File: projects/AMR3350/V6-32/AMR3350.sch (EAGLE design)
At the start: 241 parts, among them IC1 LDO-TS1117CW-3V3, IC10 TMC21X0-LA, IC11 74LS32D, IC2 ATSAM4S8C, IC3 SI87XXIS, IC4 74HC125, IC5 74S08D, IC6 TMC21X0-LA, IC7 TMC21X0-LA, IC8 TMC21X0-LA, IC9 TMC21X0-LA, J1 MOLEX-105162-001, J2 MSTBV4, Q1 NX138BKS, Q2 NX138BKS, Q3 BUK9Y53-100B, Q4 BUK9Y53-100B, U1 A4403, X1 USB-B_TH, X2 12MHz, X3 KK-254-2, X4 KK-254-4, X5 KK-254-4, X6 KK-254-4, X7 KK-254-4, X8 KK-254-4, X9 KK-254-4

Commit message: More progress
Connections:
- net FAN1_D1 renamed FAN3_D
- net FAN1_G1 renamed FAN3_G
- net FAN2_D1 renamed FAN4_D
- net FAN2_G1 renamed FAN4_G
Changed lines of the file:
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@@
 <grid distance="0.1" unitdist="inch" unit="inch" style="lines" multiple="1" display="no" altdistance="0.01" altunitdist="inch" altunit="inch"/>
 <layers>
-<layer number="1" name="Top" color="4" fill="1" visible="yes" active="no"/>
-<layer number="2" name="Route2" color="16" fill="1" visible="yes" active="no"/>
-<layer number="3" name="Route3" color="17" fill="1" visible="yes" active="no"/>
-<layer number="4" name="Route4" color="18" fill="1" visible="yes" active="no"/>
-<layer number="5" name="Route5" color="19" fill="1" visible="yes" active="no"/>
-<layer number="6" name="Route6" color="25" fill="1" visible="yes" active="no"/>
-<layer number="7" name="Route7" color="26" fill="1" visible="yes" active="no"/>
-<layer number="8" name="Route8" color="27" fill="1" visible="yes" active="no"/>
-<layer number="9" name="Route9" color="28" fill="1" visible="yes" active="no"/>
-<layer number="10" name="Route10" color="29" fill="1" visible="yes" active="no"/>
-<layer number="11" name="Route11" color="30" fill="1" visible="yes" active="no"/>
-<layer number="12" name="Route12" color="20" fill="1" visible="yes" active="no"/>
-<layer number="13" name="Route13" color="21" fill="1" visible="yes" active="no"/>
-<layer number="14" name="Route14" color="22" fill="1" visible="yes" active="no"/>
-<layer number="15" name="Route15" color="23" fill="1" visible="yes" active="no"/>
-<layer number="16" name="Bottom" color="1" fill="1" visible="yes" active="no"/>
-<layer number="17" name="Pads" color="2" fill="1" visible="yes" active="no"/>
-<layer number="18" name="Vias" color="2" fill="1" visible="yes" active="no"/>
-<layer number="19" name="Unrouted" color="6" fill="1" visible="yes" active="no"/>
-<layer number="20" name="Dimension" color="24" fill="1" visible="yes" active="no"/>
-<layer number="21" name="tPlace" color="7" fill="1" visible="yes" active="no"/>
-<layer number="22" name="bPlace" color="7" fill="1" visible="yes" active="no"/>
-<layer number="23" name="tOrigins" color="15" fill="1" visible="yes" active="no"/>
-<layer number="24" name="bOrigins" color="15" fill="1" visible="yes" active="no"/>
-<layer number="25" name="tNames" color="7" fill="1" visible="yes" active="no"/>
-<layer number="26" name="bNames" color="7" fill="1" visible="yes" active="no"/>
-<layer number="27" name="tValues" color="7" fill="1" visible="yes" active="no"/>
-<layer number="28" name="bValues" color="7" fill="1" visible="yes" active="no"/>
+<layer number="1" name="Top" color="4" fill="1" visible="no" active="no"/>
+<layer number="2" name="Route2" color="16" fill="1" visible="no" active="no"/>
+<layer number="3" name="Route3" color="17" fill="1" visible="no" active="no"/>
+<layer number="4" name="Route4" color="18" fill="1" visible="no" active="no"/>
+<layer number="5" name="Route5" color="19" fill="1" visible="no" active="no"/>
+<layer number="6" name="Route6" color="25" fill="1" visible="no" active="no"/>
+<layer number="7" name="Route7" color="26" fill="1" visible="no" active="no"/>
+<layer number="8" name="Route8" color="27" fill="1" visible="no" active="no"/>
+<layer number="9" name="Route9" color="28" fill="1" visible="no" active="no"/>
+<layer number="10" name="Route10" color="29" fill="1" visible="no" active="no"/>
+<layer number="11" name="Route11" color="30" fill="1" visible="no" active="no"/>
+<layer number="12" name="Route12" color="20" fill="1" visible="no" active="no"/>
+<layer number="13" name="Route13" color="21" fill="1" visible="no" active="no"/>
+<layer number="14" name="Route14" color="22" fill="1" visible="no" active="no"/>
+<layer number="15" name="Route15" color="23" fill="1" visible="no" active="no"/>
+<layer number="16" name="Bottom" color="1" fill="1" visible="no" active="no"/>
+<layer number="17" name="Pads" color="2" fill="1" visible="no" active="no"/>
+<layer number="18" name="Vias" color="2" fill="1" visible="no" active="no"/>
+<layer number="19" name="Unrouted" color="6" fill="1" visible="no" active="no"/>
+<layer number="20" name="Dimension" color="24" fill="1" visible="no" active="no"/>
+<layer number="21" name="tPlace" color="7" fill="1" visible="no" active="no"/>
+<layer number="22" name="bPlace" color="7" fill="1" visible="no" active="no"/>
+<layer number="23" name="tOrigins" color="15" fill="1" visible="no" active="no"/>
+<layer number="24" name="bOrigins" color="15" fill="1" visible="no" active="no"/>
+<layer number="25" name="tNames" color="7" fill="1" visible="no" active="no"/>
+<layer number="26" name="bNames" color="7" fill="1" visible="no" active="no"/>
+<layer number="27" name="tValues" color="7" fill="1" visible="no" active="no"/>
+<layer number="28" name="bValues" color="7" fill="1" visible="no" active="no"/>
 <layer number="29" name="tStop" color="7" fill="3" visible="no" active="no"/>
 <layer number="30" name="bStop" color="7" fill="6" visible="no" active="no"/>
@@
 <layer number="35" name="tGlue" color="7" fill="4" visible="no" active="no"/>
 <layer number="36" name="bGlue" color="7" fill="5" visible="no" active="no"/>
-<layer number="37" name="tTest" color="7" fill="1" visible="yes" active="no"/>
-<layer number="38" name="bTest" color="7" fill="1" visible="yes" active="no"/>
+<layer number="37" name="tTest" color="7" fill="1" visible="no" active="no"/>
+<layer number="38" name="bTest" color="7" fill="1" visible="no" active="no"/>
 <layer number="39" name="tKeepout" color="4" fill="11" visible="no" active="no"/>
 <layer number="40" name="bKeepout" color="1" fill="11" visible="no" active="no"/>
@@
 <layer number="44" name="Drills" color="7" fill="1" visible="no" active="no"/>
 <layer number="45" name="Holes" color="7" fill="1" visible="no" active="no"/>
-<layer number="46" name="Milling" color="3" fill="1" visible="yes" active="no"/>
-<layer number="47" name="Measures" color="7" fill="1" visible="yes" active="no"/>
-<layer number="48" name="Document" color="7" fill="1" visible="yes" active="no"/>
-<layer number="49" name="Reference" color="7" fill="1" visible="yes" active="no"/>
-<layer number="50" name="dxf" color="7" fill="1" visible="yes" active="no"/>
-<layer number="51" name="tDocu" color="7" fill="1" visible="yes" active="no"/>
-<layer number="52" name="bDocu" color="7" fill="1" visible="yes" active="no"/>
-<layer number="53" name="tGND_GNDA" color="7" fill="9" visible="yes" active="no"/>
-<layer number="54" name="bGND_GNDA" color="1" fill="9" visible="yes" active="no"/>
-<layer number="56" name="wert" color="7" fill="1" visible="yes" active="no"/>
-<layer number="57" name="tCAD" color="7" fill="1" visible="yes" active="no"/>
-<layer number="59" name="tCarbon" color="7" fill="1" visible="yes" active="no"/>
-<layer number="60" name="bCarbon" color="7" fill="1" visible="yes" active="no"/>
+<layer number="46" name="Milling" color="3" fill="1" visible="no" active="no"/>
+<layer number="47" name="Measures" color="7" fill="1" visible="no" active="no"/>
+<layer number="48" name="Document" color="7" fill="1" visible="no" active="no"/>
+<layer number="49" name="Reference" color="7" fill="1" visible="no" active="no"/>
+<layer number="50" name="dxf" color="7" fill="1" visible="no" active="no"/>
+<layer number="51" name="tDocu" color="7" fill="1" visible="no" active="no"/>
+<layer number="52" name="bDocu" color="7" fill="1" visible="no" active="no"/>
+<layer number="53" name="tGND_GNDA" color="7" fill="9" visible="no" active="no"/>
+<layer number="54" name="bGND_GNDA" color="1" fill="9" visible="no" active="no"/>
+<layer number="56" name="wert" color="7" fill="1" visible="no" active="no"/>
+<layer number="57" name="tCAD" color="7" fill="1" visible="no" active="no"/>
+<layer number="59" name="tCarbon" color="7" fill="1" visible="no" active="no"/>
+<layer number="60" name="bCarbon" color="7" fill="1" visible="no" active="no"/>
 <layer number="88" name="SimResults" color="9" fill="1" visible="yes" active="yes"/>
 <layer number="89" name="SimProbes" color="9" fill="1" visible="yes" active="yes"/>
@@
 </segment>
 </net>
-<net name="FAN2_D1" class="0">
+<net name="FAN4_D" class="0">
 <segment>
 <wire x1="868.68" y1="33.02" x2="901.7" y2="33.02" width="0.1524" layer="91"/>
@@
 </segment>
 </net>
-<net name="FAN1_D1" class="0">
+<net name="FAN3_D" class="0">
 <segment>
 <wire x1="868.68" y1="48.26" x2="901.7" y2="48.26" width="0.1524" layer="91"/>
@@
 </segment>
 </net>
-<net name="FAN1_G1" class="0">
+<net name="FAN3_G" class="0">
 <segment>
 <wire x1="863.6" y1="40.64" x2="861.06" y2="40.64" width="0.1524" layer="91"/>
@@
 </segment>
 </net>
-<net name="FAN2_G1" class="0">
+<net name="FAN4_G" class="0">
 <segment>
 <wire x1="863.6" y1="25.4" x2="861.06" y2="25.4" width="0.1524" layer="91"/>

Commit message: Some traces
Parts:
- added F2, F3: (no value), fuse:19560
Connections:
- net EXT_D renamed EXT1_D
- net EXT_G renamed EXT1_G
- removed net ADVREF1: C24.1, IC2.ADVREF, L4.1
- new net N$1: F2.2, J2-2.1
- new net N$2: F3.2, J2-4.1
- new net N$3: X6-1.S, X9-2.S
- new net N$4: X6-4.S, X9-3.S
- net +12V: now also F2.1, F3.1; no longer J2-2.1, J2-4.1
- net A1_Z: no longer X6-1.S
- net A2_Z: no longer X9-2.S
- net ADVREF: now also C24.1, IC2.ADVREF, L4.1
- net B1_Z: no longer X9-3.S
- net B2_Z: no longer X6-4.S
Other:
- moved on the sheet: J2-1, J2-2, J2-3, J2-4, X6-1, X6-2, X6-3, X6-4

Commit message: Almost done*
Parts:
- D1: device diode:SCHOTTKY-DIODESMC -> diode:SCHOTTKY-DIODESMD
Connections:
- removed net N$6: IC11A.O, IC11C.I1
- new net ESP_RST: ESP1.RESET, R18.2, R22.2
- new net N$5: IC11B.O, IC11C.I1
- net ESP_RESET: no longer ESP1.RESET, R18.2, R22.2
- net GND: now also IC5C.I0, IC5C.I1; no longer IC5A.I0, IC5A.I1
- net LCD_CS: now also IC5A.I1; no longer IC5C.I1
- net LCD_ENC_A: now also IC2.TCK/SWCLK/PB7; no longer IC2.PC20
- net LCD_ENC_B: now also IC2.PC20; no longer IC2.TCK/SWCLK/PB7
- net LCD_MOSI: now also IC5A.I0; no longer IC5C.I0
- net LCD_MOSI_BUF: now also IC5A.O; no longer IC5C.O
- net N$7: now also IC11A.O; no longer IC11B.O
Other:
- moved on the sheet: IC5A, IC5C

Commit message: Almost** done*
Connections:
- net BED: now also IC2.PC22; no longer IC2.PC0
- net ESP_DATA_RDY: now also IC2.PC26; no longer IC2.PC3
- net FAN_E1: now also IC2.PC3; no longer IC2.PB13/DAC0
- net FAN_E2: now also IC2.PC0; no longer IC2.PC22
- net PWR_FAIL_DET2: now also IC2.PC30/AD14; no longer IC2.PC12/AD12
- net X_STOP: now also IC2.PC16
- net Y_STOP: now also IC2.PA0/PGMEN0
- net Z_STOP: now also IC2.PC17

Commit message: Done***
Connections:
- net RESET: now also RESET.P1; no longer RESET.P
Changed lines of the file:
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@@
 <wire x1="332.74" y1="-33.02" x2="332.74" y2="-30.48" width="0.1524" layer="91"/>
 <junction x="332.74" y="-30.48"/>
-<pinref part="RESET" gate="G$1" pin="P"/>
-<wire x1="332.74" y1="-30.48" x2="332.74" y2="-27.94" width="0.1524" layer="91"/>
-<wire x1="332.74" y1="-27.94" x2="335.28" y2="-27.94" width="0.1524" layer="91"/>
 <label x="297.18" y="-30.48" size="1.778" layer="95"/>
+<pinref part="RESET" gate="G$1" pin="P1"/>
+<wire x1="332.74" y1="-30.48" x2="335.28" y2="-30.48" width="0.1524" layer="91"/>
 </segment>
 </net>

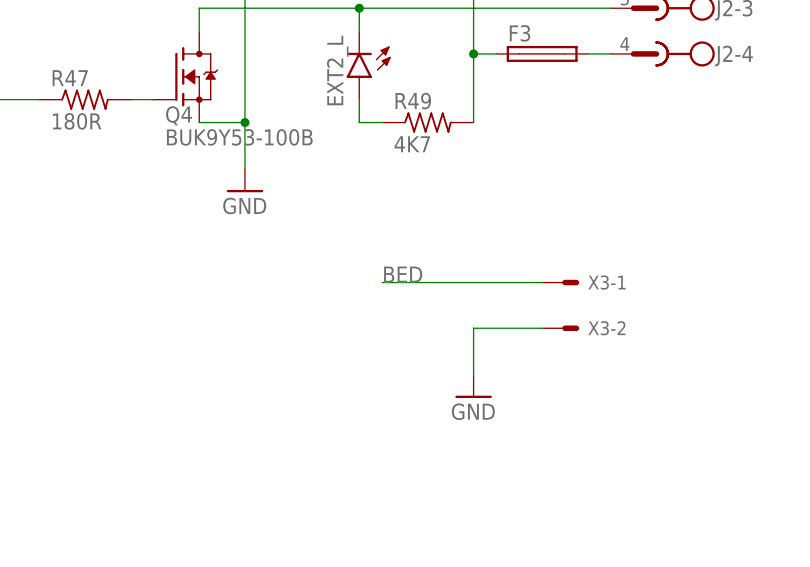
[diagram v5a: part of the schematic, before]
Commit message: Added a resistor
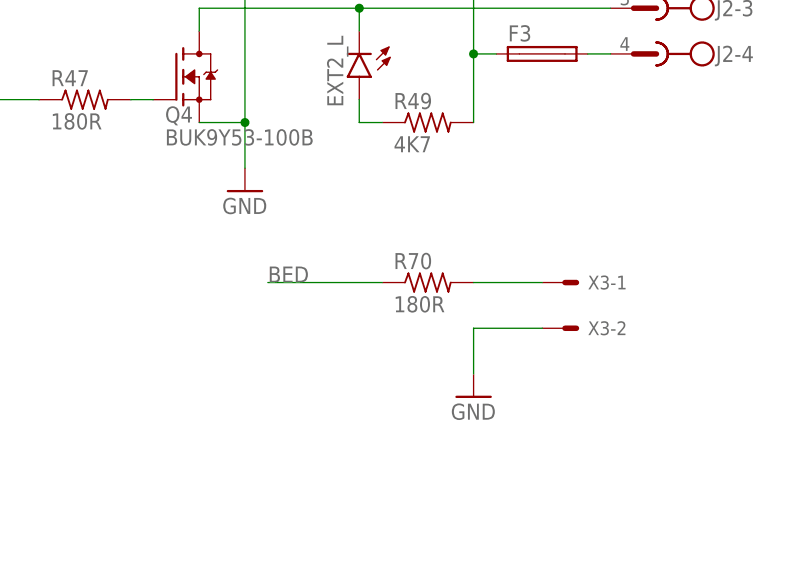
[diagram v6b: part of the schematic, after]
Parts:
- added R70: 180R, resistor:R-US_R0603
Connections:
- new net BED_OUT: R70.2, X3-1.S
- net BED: now also R70.1; no longer X3-1.S

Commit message: Properly positioned names/labels (silkscreen)
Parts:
- removed U1: A4403, misc:A4403
- removed X1: USB-B_TH, SmartPrj:PN61729
- added IC12: 74LS32D, 74xx-us:74LS32D
- added USB_L: (no value), led:LEDCHIPLED_0805
- IC1: value LDO-TS1117CW-3V3 -> A4403; device we-power:LDO-TS1117CW-3V3 -> misc:A4403
- IC11: value 74LS32D -> TMC21X0-LA; device 74xx-us:74LS32D -> SilentStepStick-TMC2130_v11:TMC21X0-LA
- IC2: value ATSAM4S8C -> LDO-TS1117CW-3V3; device misc:ATSAM4S8C -> we-power:LDO-TS1117CW-3V3
- IC3: value SI87XXIS -> ATSAM4S8C; device misc:SI87XXIS -> misc:ATSAM4S8C
- IC4: value 74HC125 -> SI87XXIS; device misc:74HC125 -> misc:SI87XXIS
- IC5: value 74S08D -> 74HC125; device 74xx-us:74S08D -> misc:74HC125
- IC6: value TMC21X0-LA -> 74S08D; device SilentStepStick-TMC2130_v11:TMC21X0-LA -> 74xx-us:74S08D
- R50: value 0R11 -> 180R; device resistor:R-US_R1206 -> resistor:R-US_R0603
- R52, R56, R60, R64, R68: value 20K -> 0R11; device resistor:R-TRIMM3103 -> resistor:R-US_R1206
- R53, R57, R61, R65, R69: device resistor:R-US_R0603 -> resistor:R-TRIMM3103
- R54, R58, R62, R66: value 0R11 -> 20K; device resistor:R-US_R1206 -> resistor:R-US_R0603
- R70: value 180R -> 20K
- USB: value (none) -> USB-B_TH; device led:LEDCHIPLED_0805 -> SmartPrj:PN61729
- renumbered 3V1 to 3V3, ESP1 to ESP8266
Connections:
- net ESP_URDX renamed ESP_RXD
- net ESP_UTDX renamed ESP_TXD
- net N$1 renamed E1_FUSED
- net N$2 renamed E2_FUSED
- net N$55 renamed IDEK
- removed net N$3: X6-1.S, X9-2.S
- removed net N$4: X6-4.S, X9-3.S
- removed net N$5: IC11B.O, IC11C.I1
- removed net N$7: IC11A.O, IC11D.I0
- removed net N$8: IC11C.O, IC11D.I1
- new net AMID_Z: X6-1.S, X7-2.S
- new net BMID_Z: X6-4.S, X7-3.S
- new net SG_TST_E1Z: IC12B.O, IC12C.I1
- new net SG_TST_XY: IC12A.O, IC12D.I0
- new net SG_TST_ZE: IC12C.O, IC12D.I1
- net +12V: now also IC11.VS, IC11.VSA; no longer IC6.VS, IC6.VSA
- net +3V3: now also IC11.VCC_IO, IC12P.VCC, IC2.VO, IC3.VDDIN, IC3.VDDIO-27, IC3.VDDIO-50, IC3.VDDIO-69, IC3.VDDIO-91, IC3.VDDIO-98, IC4.VDD, IC5P.VCC; no longer IC1.VO, IC11P.VCC, IC2.VDDIN, IC2.VDDIO-27, IC2.VDDIO-50, IC2.VDDIO-69, IC2.VDDIO-91, IC2.VDDIO-98, IC3.VDD, IC4P.VCC, IC6.VCC_IO
- net +5V: now also IC11.VCC, IC2.VI, IC6P.VCC, R54.2, R58.2, R62.2, R66.2, R70.2; no longer IC1.VI, IC5P.VCC, IC6.VCC, R53.2, R57.2, R61.2, R65.2, R69.2
- net 5V_E1: now also IC10.5VOUT; no longer IC9.5VOUT
- net 5V_E2: now also IC11.5VOUT; no longer IC10.5VOUT
- net 5V_X: now also IC7.5VOUT; no longer IC6.5VOUT
- net 5V_Y: now also IC8.5VOUT; no longer IC7.5VOUT
- net 5V_Z: now also IC9.5VOUT; no longer IC8.5VOUT
- net A1_E1: now also IC10.OA1, X8-1.S; no longer IC9.OA1, X7-1.S
- net A1_E2: now also IC11.OA1, X9-1.S; no longer IC10.OA1, X8-1.S
- net A1_X: now also IC7.OA1; no longer IC6.OA1
- net A1_Y: now also IC8.OA1; no longer IC7.OA1
- net A1_Z: now also IC9.OA1, X7-1.S; no longer IC8.OA1, X9-1.S
- net A2_E1: now also IC10.OA2, X8-2.S; no longer IC9.OA2, X7-2.S
- net A2_E2: now also IC11.OA2, X9-2.S; no longer IC10.OA2, X8-2.S
- net A2_X: now also IC7.OA2; no longer IC6.OA2
- net A2_Y: now also IC8.OA2; no longer IC7.OA2
- net A2_Z: now also IC9.OA2; no longer IC8.OA2
- net ADVREF: now also IC3.ADVREF; no longer IC2.ADVREF
- net B1_E1: now also IC10.OB1, X8-3.S; no longer IC9.OB1, X7-3.S
- net B1_E2: now also IC11.OB1, X9-3.S; no longer IC10.OB1, X8-3.S
- net B1_X: now also IC7.OB1; no longer IC6.OB1
- net B1_Y: now also IC8.OB1; no longer IC7.OB1
- net B1_Z: now also IC9.OB1; no longer IC8.OB1
- net B2_E1: now also IC10.OB2, X8-4.S; no longer IC9.OB2, X7-4.S
- net B2_E2: now also IC11.OB2, X9-4.S; no longer IC10.OB2, X8-4.S
- net B2_X: now also IC7.OB2; no longer IC6.OB2
- net B2_Y: now also IC8.OB2; no longer IC7.OB2
- net B2_Z: now also IC9.OB2, X7-4.S; no longer IC8.OB2, X9-4.S
- net BED: now also IC3.PC22, R50.1; no longer IC2.PC22, R70.1
- net BED_OUT: now also R50.2; no longer R70.2
- net BOOT: now also IC1.BOOT; no longer U1.BOOT
- net BRA_E1: now also IC10.BRA, R63.1; no longer IC9.BRA, R62.1
- net BRA_E2: now also IC11.BRA, R67.1; no longer IC10.BRA, R66.1
- net BRA_X: now also IC7.BRA, R51.1; no longer IC6.BRA, R50.1
- net BRA_Y: now also IC8.BRA, R55.1; no longer IC7.BRA, R54.1
- net BRA_Z: now also IC9.BRA, R59.1; no longer IC8.BRA, R58.1
- net BRB_E1: now also IC10.BRB, R64.1; no longer IC9.BRB, R63.1
- net BRB_E2: now also IC11.BRB, R68.1; no longer IC10.BRB, R67.1
- net BRB_X: now also IC7.BRB, R52.1; no longer IC6.BRB, R51.1
- net BRB_Y: now also IC8.BRB, R56.1; no longer IC7.BRB, R55.1
- net BRB_Z: now also IC9.BRB, R60.1; no longer IC8.BRB, R59.1
- net CPI_E1: now also IC10.CPI; no longer IC9.CPI
- net CPI_E2: now also IC11.CPI; no longer IC10.CPI
- net CPI_X: now also IC7.CPI; no longer IC6.CPI
- net CPI_Y: now also IC8.CPI; no longer IC7.CPI
- net CPI_Z: now also IC9.CPI; no longer IC8.CPI
- net CPO_E1: now also IC10.CPO; no longer IC9.CPO
- net CPO_E2: now also IC11.CPO; no longer IC10.CPO
- net CPO_X: now also IC7.CPO; no longer IC6.CPO
- net CPO_Y: now also IC8.CPO; no longer IC7.CPO
- net CPO_Z: now also IC9.CPO; no longer IC8.CPO
- net E1_DIR: now also IC10.REFR_DIR, IC3.TDI/PB4; no longer IC2.TDI/PB4, IC9.REFR_DIR
- net E1_EN: now also IC10.CSN_CFG3, IC3.PA4/PGMNCMD; no longer IC2.PA4/PGMNCMD, IC9.CSN_CFG3
- net E1_STEP: now also IC10.REFL_STEP, IC3.PC28; no longer IC2.PC28, IC9.REFL_STEP
- net E2_DIR: now also IC11.REFR_DIR, IC3.PC9; no longer IC10.REFR_DIR, IC2.PC9
- net E2_EN: now also IC11.CSN_CFG3, IC3.PA3; no longer IC10.CSN_CFG3, IC2.PA3
- net E2_STEP: now also IC11.REFL_STEP, IC3.PC10; no longer IC10.REFL_STEP, IC2.PC10
- net ENN: now also IC11.DRV_ENN_CFG6, IC3.PC14; no longer IC2.PC14, IC6.DRV_ENN_CFG6
- net ERASE: now also IC3.ERASE/PB12; no longer IC2.ERASE/PB12
- net ESP_DATA_RDY: now also IC3.PC26; no longer IC2.PC26
- net ESP_EN: now also IC3.PC6; no longer IC2.PC6
- net ESP_MISO: now also IC3.PA12/PGMD0; no longer IC2.PA12/PGMD0
- net ESP_MOSI: now also IC3.PA13/PGMD1; no longer IC2.PA13/PGMD1
- net ESP_NPCS0: now also IC3.PA11/PGMM3; no longer IC2.PA11/PGMM3
- net ESP_RESET: now also IC3.PC2; no longer IC2.PC2
- net ESP_SCK: now also IC3.PA14/PGMD2; no longer IC2.PA14/PGMD2
- net ESP_URXD: now also IC3.PA9/PGMM1; no longer IC2.PA9/PGMM1
- net ESP_UTXD: now also IC3.PA10/PGMM2; no longer IC2.PA10/PGMM2
- net EXT1: now also IC3.PA20/PGMD8/AD3; no longer IC2.PA20/PGMD8/AD3
- net EXT2: now also IC3.PC15/AD11; no longer IC2.PC15/AD11
- net FAN_E1: now also IC3.PC3; no longer IC2.PC3
- net FAN_E2: now also IC3.PC0; no longer IC2.PC0
- net FAN_MOBO: now also IC3.PA18/PGMD6/AD1; no longer IC2.PA18/PGMD6/AD1
- net FAN_PART: now also IC3.PC13/AD10; no longer IC2.PC13/AD10
- net FB: now also IC1.FB; no longer U1.FB
- net GND: now also IC1.DIS, IC1.NC13, IC1.NC14, IC1.NC15, IC1.NC16, IC1.NC2, IC1.NC7, IC1.PAD, IC11.CLK, IC11.ENCB_DCEN_CFG4, IC11.GND, IC11.GNDA, IC11.TST_MODE, IC12P.GND, IC2.GND, IC3.GND-2, IC3.GND-26, IC3.GND-45, IC3.GND-70, IC3.GND-95, IC3.JTAGSEL, IC3.TST, IC4.C1, IC4.GND, IC5A.OE, IC5B.OE, IC5D.I, IC5D.OE, IC6C.I0, IC6C.I1, IC6P.GND, R52.2, R53.E, R56.2, R57.E, R60.2, R61.E, R64.2, R65.E, R68.2, R69.E, USB.4, USB.P$1, USB.P$2; no longer IC11P.GND, IC2.GND-2, IC2.GND-26, IC2.GND-45, IC2.GND-70, IC2.GND-95, IC2.JTAGSEL, IC2.TST, IC3.C1, IC3.GND, IC4A.OE, IC4B.OE, IC4D.I, IC4D.OE, IC4P.GND, IC5C.I0, IC5C.I1, IC6.CLK, IC6.ENCB_DCEN_CFG4, IC6.GND, IC6.GNDA, IC6.TST_MODE, R50.2, R52.E, R54.2, R56.E, R58.2, R60.E, R62.2, R64.E, R66.2, R68.E, U1.DIS, U1.GND, U1.NC13, U1.NC14, U1.NC15, U1.NC16, U1.NC2, U1.NC7, U1.PAD, X1.4, X1.P$1, X1.P$2
- net IREF_E1: now also IC10.AIN_IREF, R65.S; no longer IC9.AIN_IREF, R64.S
- net IREF_E2: now also IC11.AIN_IREF, R69.S; no longer IC10.AIN_IREF, R68.S
- net IREF_X: now also IC7.AIN_IREF, R53.S; no longer IC6.AIN_IREF, R52.S
- net IREF_Y: now also IC8.AIN_IREF, R57.S; no longer IC7.AIN_IREF, R56.S
- net IREF_Z: now also IC9.AIN_IREF, R61.S; no longer IC8.AIN_IREF, R60.S
- net ISEN: now also IC1.ISEN; no longer U1.ISEN
- net LCD_BEEP: now also IC3.PC23; no longer IC2.PC23
- net LCD_CS: now also IC3.PC19, IC6A.I1, IC6B.I0, IC6B.I1, IC6D.I1; no longer IC2.PC19, IC5A.I1, IC5B.I0, IC5B.I1, IC5D.I1
- net LCD_CS_BUF: now also IC6B.O; no longer IC5B.O
- net LCD_ENC_A: now also IC3.TCK/SWCLK/PB7; no longer IC2.TCK/SWCLK/PB7
- net LCD_ENC_B: now also IC3.PC20; no longer IC2.PC20
- net LCD_ENC_SW: now also IC3.PC21; no longer IC2.PC21
- net LCD_MISO: now also IC3.PA5/PGMRDY, IC5C.O; no longer IC2.PA5/PGMRDY, IC4C.O
- net LCD_MISO_BUF: now also IC5C.I; no longer IC4C.I
- net LCD_MOSI: now also IC3.PB6/PGMNOE, IC5A.I, IC6A.I0; no longer IC2.PB6/PGMNOE, IC4A.I, IC5A.I0
- net LCD_MOSI_BUF: now also IC6A.O; no longer IC5A.O
- net LCD_SCK: now also IC3.PA2/PGMEN2, IC5B.I, IC6D.I0; no longer IC2.PA2/PGMEN2, IC4B.I, IC5D.I0
- net LCD_SCK_BUF: now also IC6D.O; no longer IC5D.O
- net LCD_SD_CS: now also IC3.PB14/DAC1, IC5C.OE; no longer IC2.PB14/DAC1, IC4C.OE
- net LX: now also IC1.LX; no longer U1.LX
- net MCCDA: now also IC3.PA28; no longer IC2.PA28
- net MCCK: now also IC3.PA29; no longer IC2.PA29
- net MCDA0: now also IC3.PA30; no longer IC2.PA30
- net MCDA1: now also IC3.PA31; no longer IC2.PA31
- net MCDA2: now also IC3.PA26/PGMD14; no longer IC2.PA26/PGMD14
- net MCDA3: now also IC3.PA27/PGMD15; no longer IC2.PA27/PGMD15
- net MOT_MISO: now also IC11.SDO_NAO_CFG0, IC3.PA21/PGMD9/AD8; no longer IC2.PA21/PGMD9/AD8, IC6.SDO_NAO_CFG0
- net MOT_MOSI: now also IC11.SDI_NAI_CFG1, IC3.PA22/PGMD10/AD9; no longer IC2.PA22/PGMD10/AD9, IC6.SDI_NAI_CFG1
- net MOT_SCK: now also IC11.SCK_CFG2, IC3.PA23/PGMD11; no longer IC2.PA23/PGMD11, IC6.SCK_CFG2
- net PWR_FAIL_DET2: now also IC3.PC30/AD14; no longer IC2.PC30/AD14
- net REFIN_E1: now also R65.A, R66.1; no longer R64.A, R65.1
- net REFIN_E2: now also R69.A, R70.1; no longer R68.A, R69.1
- net REFIN_X: now also R53.A, R54.1; no longer R52.A, R53.1
- net REFIN_Y: now also R57.A, R58.1; no longer R56.A, R57.1
- net REFIN_Z: now also R61.A, R62.1; no longer R60.A, R61.1
- net RESET: now also IC3.NRST; no longer IC2.NRST
- net SAM_TFR_RDY: now also IC3.PA7/XIN32/PGMNVALID; no longer IC2.PA7/XIN32/PGMNVALID
- net SD_CD: now also IC3.PC8; no longer IC2.PC8
- net SD_MOSI_BUF: now also IC5A.O; no longer IC4A.O
- net SD_SCK_BUF: now also IC5B.O; no longer IC4B.O
- net SGND: now also IC1.SGND; no longer U1.SGND
- net SG_TST: now also IC12D.O, IC3.PA1/PGMEN1; no longer IC11D.O, IC2.PA1/PGMEN1
- net SG_TST_E1: now also IC10.SWP_DIAG1, IC12B.I1; no longer IC11B.I1, IC9.SWP_DIAG1
- net SG_TST_E2: now also IC11.SWP_DIAG1, IC12C.I0; no longer IC10.SWP_DIAG1, IC11C.I0
- net SG_TST_X: now also IC12A.I0, IC7.SWP_DIAG1; no longer IC11A.I0, IC6.SWP_DIAG1
- net SG_TST_Y: now also IC12A.I1, IC8.SWP_DIAG1; no longer IC11A.I1, IC7.SWP_DIAG1
- net SG_TST_Z: now also IC12B.I0, IC9.SWP_DIAG1; no longer IC11B.I0, IC8.SWP_DIAG1
- net SS: now also IC1.SS; no longer U1.SS
- net TON: now also IC1.TON; no longer U1.TON
- net T_BED: now also IC3.PB1/AD5; no longer IC2.PB1/AD5
- net T_EXT1: now also IC3.PB0/AD4; no longer IC2.PB0/AD4
- net T_EXT2: now also IC3.PC29/AD13; no longer IC2.PC29/AD13
- net USB_LED: now also USB_L.C; no longer USB.C
- net USB_N: now also IC3.DDM/PB10, USB.2; no longer IC2.DDM/PB10, X1.2
- net USB_P: now also IC3.DDP/PB11, USB.3; no longer IC2.DDP/PB11, X1.3
- net USB_PWR_MON: now also IC3.PC11; no longer IC2.PC11
- net VBUS: now also USB.1, USB_L.A; no longer USB.A, X1.1
- net VCP_E1: now also IC10.VCP; no longer IC9.VCP
- net VCP_E2: now also IC11.VCP; no longer IC10.VCP
- net VCP_X: now also IC7.VCP; no longer IC6.VCP
- net VCP_Y: now also IC8.VCP; no longer IC7.VCP
- net VCP_Z: now also IC9.VCP; no longer IC8.VCP
- net VDDOUT: now also IC3.VDDCORE-16, IC3.VDDCORE-36, IC3.VDDCORE-56, IC3.VDDCORE-85, IC3.VDDOUT; no longer IC2.VDDCORE-16, IC2.VDDCORE-36, IC2.VDDCORE-56, IC2.VDDCORE-85, IC2.VDDOUT
- net VDDPLL: now also IC3.VDDPLL; no longer IC2.VDDPLL
- net VIN_F: now also IC1.VIN; no longer U1.VIN
- net VREF_MON: now also IC3.PA17/PGMD5/AD0; no longer IC2.PA17/PGMD5/AD0
- net VSSA_MON: now also IC3.PA19/PGMD7/AD2; no longer IC2.PA19/PGMD7/AD2
- net XIN: now also IC3.PB9/PGMCK/XIN; no longer IC2.PB9/PGMCK/XIN
- net XOUT: now also IC3.PB8/XOUT; no longer IC2.PB8/XOUT
- net X_DIR: now also IC3.PA16/PGMD4, IC7.REFR_DIR; no longer IC2.PA16/PGMD4, IC6.REFR_DIR
- net X_EN: now also IC3.PA15/PGMD3, IC7.CSN_CFG3; no longer IC2.PA15/PGMD3, IC6.CSN_CFG3
- net X_STEP: now also IC3.PC7, IC7.REFL_STEP; no longer IC2.PC7, IC6.REFL_STEP
- net X_STOP: now also IC3.PC16; no longer IC2.PC16
- net Y_DIR: now also IC3.PA24/PGMD12, IC8.REFR_DIR; no longer IC2.PA24/PGMD12, IC7.REFR_DIR
- net Y_EN: now also IC3.PC4, IC8.CSN_CFG3; no longer IC2.PC4, IC7.CSN_CFG3
- net Y_STEP: now also IC3.PC5, IC8.REFL_STEP; no longer IC2.PC5, IC7.REFL_STEP
- net Y_STOP: now also IC3.PA0/PGMEN0; no longer IC2.PA0/PGMEN0
- net Z_DIR: now also IC3.PA25/PGMD13, IC9.REFR_DIR; no longer IC2.PA25/PGMD13, IC8.REFR_DIR
- net Z_EN: now also IC3.PA8/XOUT32/PGMM0, IC9.CSN_CFG3; no longer IC2.PA8/XOUT32/PGMM0, IC8.CSN_CFG3
- net Z_STEP: now also IC3.PC1, IC9.REFL_STEP; no longer IC2.PC1, IC8.REFL_STEP
- net Z_STOP: now also IC3.PC17, IC4.OUT; no longer IC2.PC17, IC3.OUT
- net Z_STOP_IN: now also IC4.A1; no longer IC3.A1
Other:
- moved on the sheet: IC10, IC5P, IC7, IC8, IC9, R50, R51, R54, R55, R58, R59, R62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

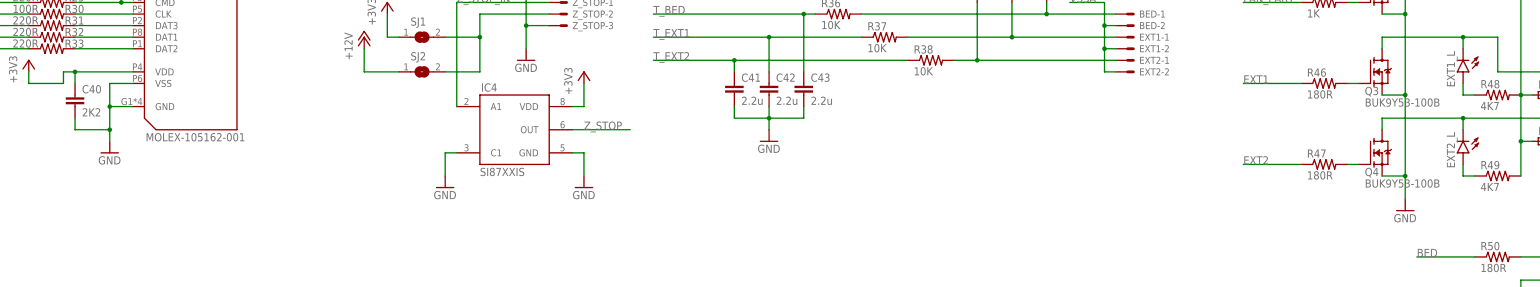
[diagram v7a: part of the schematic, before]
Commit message: Changes from a while back, which I think involved a different component choice?
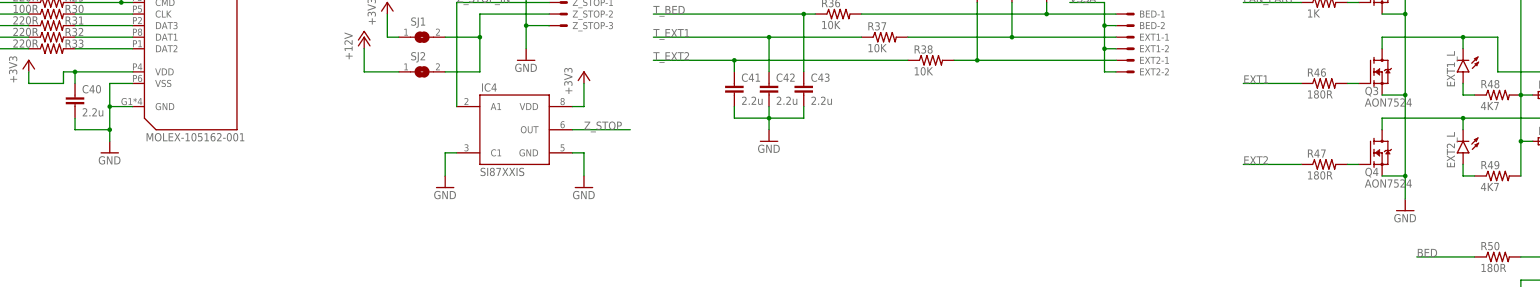
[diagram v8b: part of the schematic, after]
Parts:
- C40: value 2K2 -> 2.2u
- Q3, Q4: value BUK9Y53-100B -> AON7524; device misc:BUK9Y53-100B -> misc:AON7524
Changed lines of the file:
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@@
 <part name="+3V7" library="supply1" library_urn="urn:adsk.eagle:library:371" deviceset="+3V3" device=""/>
 <part name="GND25" library="supply1" library_urn="urn:adsk.eagle:library:371" deviceset="GND" device=""/>
-<part name="C40" library="resistor" library_urn="urn:adsk.eagle:library:348" deviceset="C-EU" device="C0603" package3d_urn="urn:adsk.eagle:package:23616/2" value="2K2"/>
+<part name="C40" library="resistor" library_urn="urn:adsk.eagle:library:348" deviceset="C-EU" device="C0603" package3d_urn="urn:adsk.eagle:package:23616/2" value="2.2u"/>
 <part name="+3V8" library="supply1" library_urn="urn:adsk.eagle:library:371" deviceset="+3V3" device=""/>
 <part name="R34" library="resistor" library_urn="urn:adsk.eagle:library:348" deviceset="R-US_" device="R0603" package3d_urn="urn:adsk.eagle:package:23555/3" value="10K"/>
@@
 <part name="GND1" library="supply1" library_urn="urn:adsk.eagle:library:371" deviceset="GND" device=""/>
 <part name="Q1" library="misc" deviceset="NX138BKS" device=""/>
-<part name="Q3" library="misc" deviceset="BUK9Y53-100B" device=""/>
-<part name="Q4" library="misc" deviceset="BUK9Y53-100B" device=""/>
+<part name="Q3" library="misc" deviceset="AON7524" device=""/>
+<part name="Q4" library="misc" deviceset="AON7524" device=""/>
 <part name="P+5" library="supply1" library_urn="urn:adsk.eagle:library:371" deviceset="+12V" device=""/>
 <part name="R38" library="resistor" library_urn="urn:adsk.eagle:library:348" deviceset="R-US_" device="R0603" package3d_urn="urn:adsk.eagle:package:23555/3" value="10K"/>
